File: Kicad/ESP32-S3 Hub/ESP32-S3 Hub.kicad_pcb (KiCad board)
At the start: 6 copper layers, 15 x 30 mm, 60 parts, among them J1 1.27mm 3pin socket, J10 1.27mm 3pin socket, J11 7 pin FPC 0.3mm Panasonic Y3b, J12 1.27mm 3pin socket, J13 TE 3-2363961-0 receptacle, J14 TE 3-2363962-0 Connector, J16 TE 3-2363961-0 receptacle, J17 TE 3-2363962-0 Connector, J2 1.27mm 3pin socket, J21 1.27mm 4 pin socket, J22 1.27mm 4 pin header, J3 7 pin FPC 0.3mm Panasonic Y3b, J4 1.27mm 3pin socket, J5 7 pin FPC 0.3mm Panasonic Y3b, J6 1.27mm 3pin socket, J7 1.27mm 3pin socket, J8 7 pin FPC 0.3mm Panasonic Y3b, J9 1.27mm 3pin socket, SW1 Mitsumi R-667996, SW2 Mitsumi R-667996, U1 ESP32-S3, U2 74HC595, U3 THVD1420DRLR, Y1 ABM11-40.000MHZ-B1U-T3, 10ppm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

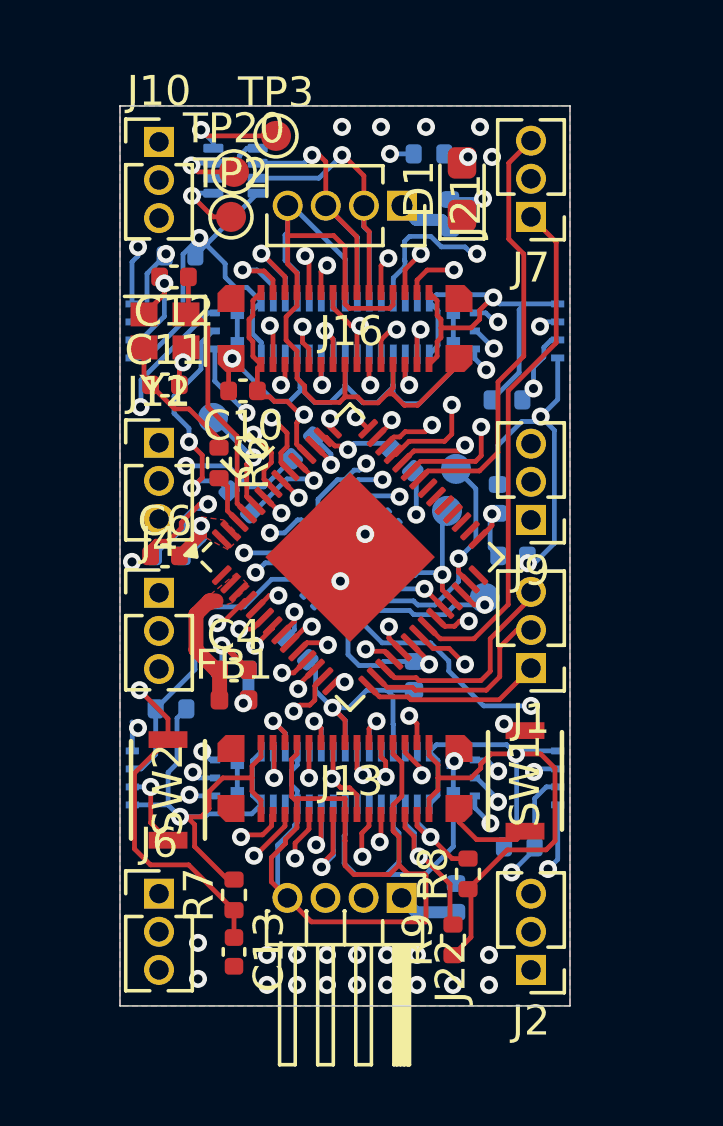
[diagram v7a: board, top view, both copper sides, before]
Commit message: Arranged Silkscreen
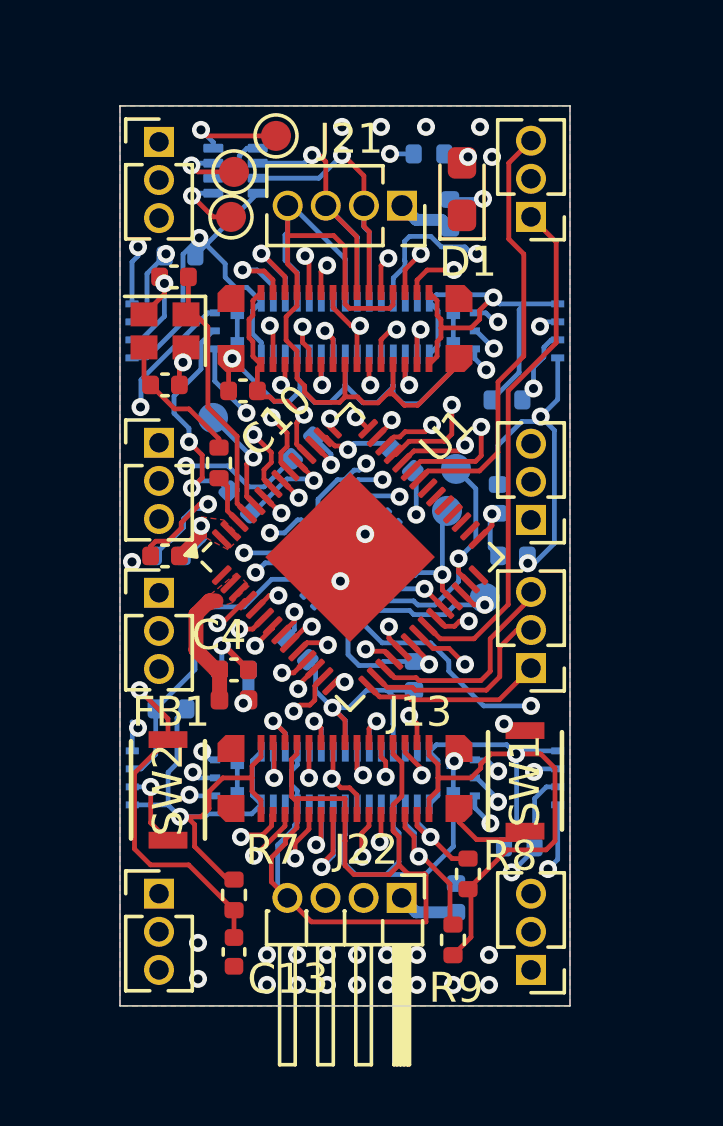
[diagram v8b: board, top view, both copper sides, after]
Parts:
- TP1: value ~ -> S-EN
- TP12: value ~ -> SRCLK
- TP14: value ~ -> SER
- TP2: value ~ -> RX
- TP3: value ~ -> TX
- TP4: value ~ -> IO46
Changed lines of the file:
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@@
 		(tags "LED handsolder")
 		(property "Reference" "D1"
-			(at 0 -1.43 90)
+			(at -2.425 0.2 180)
 			(layer "F.SilkS")
 			(effects
@@
 		(tags "Through hole angled pin header THT 1x04 1.27mm single row")
 		(property "Reference" "J22"
-			(at 2.4325 -1.635 90)
+			(at -1.6 1.19 180)
 			(layer "F.SilkS")
 			(effects
@@
 		(tags "capacitor")
 		(property "Reference" "C13"
-			(at 0 -1.16 90)
+			(at 0.9 -1.8 180)
 			(layer "F.SilkS")
 			(effects
@@
 		(tags "capacitor")
 		(property "Reference" "C10"
-			(at 0 -1.16 0)
+			(at -1.1 -1 45)
 			(layer "F.SilkS")
 			(effects
@@
 			(at 0 -1.448 0)
 			(layer "F.SilkS")
+			(hide yes)
 			(effects
 				(font
@@
 		(tags "resistor")
 		(property "Reference" "R8"
-			(at 0 -1.17 90)
+			(at 0.6 1.4 180)
 			(layer "F.SilkS")
 			(effects
@@
 			(at 0 -1.695 0)
 			(layer "F.SilkS")
+			(hide yes)
 			(effects
 				(font
@@
 			(at 0 -1.695 0)
 			(layer "F.SilkS")
+			(hide yes)
 			(effects
 				(font
@@
 		(tags "capacitor")
 		(property "Reference" "C4"
-			(at 0 -1.16 0)
+			(at -0.5 -1.16 0)
 			(layer "F.SilkS")
 			(effects
@@
 			(at 0 -1.448 0)
 			(layer "F.SilkS")
+			(hide yes)
 			(effects
 				(font
@@
 			)
 		)
-		(property "Value" "~"
+		(property "Value" "RX"
 			(at 0 1.55 0)
 			(layer "F.Fab")
@@
 			(at 0 -1.16 0)
 			(layer "F.SilkS")
+			(hide yes)
 			(effects
 				(font
@@
 			(at 0 -1.695 0)
 			(layer "F.SilkS")
+			(hide yes)
 			(effects
 				(font
@@
 			(at 0 -1.695 0)
 			(layer "F.SilkS")
+			(hide yes)
 			(effects
 				(font
@@
 		(tags "SMD SMT crystal")
 		(property "Reference" "Y1"
-			(at 0 -2.000001 0)
+			(at -1.8 -1.7 0)
 			(layer "F.SilkS")
+			(hide yes)
 			(effects
 				(font
@@
 			(at 0 -1.695 0)
 			(layer "F.SilkS")
+			(hide yes)
 			(effects
 				(font
@@
 		(tags "resistor")
 		(property "Reference" "R9"
-			(at 0 -1.17 90)
+			(at -1.6 0.1 180)
 			(layer "F.SilkS")
 			(effects
@@
 		(tags "inductor")
 		(property "Reference" "FB1"
-			(at 0 -1.17 0)
+			(at -2.1 0.4 0)
 			(layer "F.SilkS")
 			(effects
@@
 		(tags "QFN NoLead")
 		(property "Reference" "U1"
-			(at 0 -4.800001 45)
+			(at 5.140986 -0.573076 45)
 			(layer "F.SilkS")
 			(effects
@@
 			(at 0 -1.16 0)
 			(layer "F.SilkS")
+			(hide yes)
 			(effects
 				(font
@@
 			(at 0 -1.695 0)
 			(layer "F.SilkS")
+			(hide yes)
 			(effects
 				(font
@@
 		(tags "mezzanine B2B 0.4mm board-to-board receptacle")
 		(property "Reference" "J16"
-			(at 0.21 0.01 0)
+			(at 2.3 2.3 0)
 			(unlocked yes)
 			(layer "F.SilkS")
+			(hide yes)
 			(effects
 				(font
@@
 		(tags "Through hole socket strip THT 1x04 1.27mm single row")
 		(property "Reference" "J21"
-			(at 0 -2.135 90)
+			(at -2.225 1.7 180)
 			(layer "F.SilkS")
 			(effects
@@
 		(tags "resistor")
 		(property "Reference" "R7"
-			(at 0 -1.17 90)
+			(at 1.5 1.3 180)
 			(layer "F.SilkS")
 			(effects
@@
 		(tags "resistor")
 		(property "Reference" "R6"
-			(at 0 -1.17 90)
+			(at -1.5 1.1 180)
 			(layer "F.SilkS")
+			(hide yes)
 			(effects
 				(font
@@
 			(at 0 -1.695 0)
 			(layer "F.SilkS")
+			(hide yes)
 			(effects
 				(font
@@
 			(at 0 -1.695 0)
 			(layer "F.SilkS")
+			(hide yes)
 			(effects
 				(font
@@
 		(tags "capacitor")
 		(property "Reference" "C6"
-			(at 0 -1.16 360)
+			(at 0.9 1.1 90)
 			(layer "F.SilkS")
+			(hide yes)
 			(effects
 				(font
@@
 			(at 0 -1.448 0)
 			(layer "F.SilkS")
+			(hide yes)
 			(effects
 				(font
@@
 			)
 		)
-		(property "Value" "~"
+		(property "Value" "TX"
 			(at 0 1.55 0)
 			(layer "F.Fab")
@@
 		(tags "mezzanine B2B 0.4mm board-to-board receptacle")
 		(property "Reference" "J13"
-			(at 0.21 0.01 0)
+			(at 2.5 -2.3 0)
 			(unlocked yes)
 			(layer "F.SilkS")
@@
 		(tags "resistor")
 		(property "Reference" "R1"
-			(at 0 1.17 135)
+			(at 1.697056 0 135)
 			(layer "B.SilkS")
 			(effects
@@
 		(tags "resistor")
 		(property "Reference" "R10"
-			(at 0 1.17 0)
+			(at -2.3 -0.3 0)
 			(layer "B.SilkS")
 			(effects
@@
 		(tags "DHVQFN NoLead")
 		(property "Reference" "U2"
-			(at 0 3.05 135)
+			(at 2.687006 0.141421 -135)
 			(layer "B.SilkS")
 			(effects
@@
 		(tags "capacitor")
 		(property "Reference" "C9"
-			(at 0 1.16 0)
+			(at 1.5 0.1 90)
 			(layer "B.SilkS")
 			(effects
@@
 		(tags "capacitor")
 		(property "Reference" "C2"
-			(at 0 1.16 0)
+			(at -0.3 1.5 0)
 			(layer "B.SilkS")
 			(effects
@@
 		(tags "resistor")
 		(property "Reference" "R3"
-			(at 0 1.17 135)
+			(at -2.05061 0.070711 135)
 			(layer "B.SilkS")
 			(effects
@@
 			(at 0 1.448 0)
 			(layer "B.SilkS")
+			(hide yes)
 			(effects
 				(font
@@
 			)
 		)
-		(property "Value" "~"
+		(property "Value" "IO46"
 			(at 0 -1.55 0)
 			(layer "B.Fab")
@@
 		(tags "capacitor")
 		(property "Reference" "C7"
-			(at 0 1.16 90)
+			(at 1.8 0 90)
 			(layer "B.SilkS")
 			(effects
@@
 		(tags "resistor")
 		(property "Reference" "R20"
-			(at 0 1.17 0)
+			(at -2.3 0 0)
 			(layer "B.SilkS")
 			(effects
@@
 			(at 0 1.448 0)
 			(layer "B.SilkS")
+			(hide yes)
 			(effects
 				(font
@@
 			)
 		)
-		(property "Value" "~"
+		(property "Value" "SER"
 			(at 0 -1.55 0)
 			(layer "B.Fab")
@@
 		(tags "capacitor")
 		(property "Reference" "C8"
-			(at 0 1.16 90)
+			(at 0 -1.2 90)
 			(layer "B.SilkS")
 			(effects
@@
 		(tags "mezzanine B2B 0.4mm board-to-board connector")
 		(property "Reference" "J17"
-			(at 0.04 -2.33 0)
+			(at -0.2 2.3 0)
 			(unlocked yes)
 			(layer "B.SilkS")
@@
 			(at 0 1.448 0)
 			(layer "B.SilkS")
+			(hide yes)
 			(effects
 				(font
@@
 			)
 		)
-		(property "Value" "~"
+		(property "Value" "S-EN"
 			(at 0 -1.55 0)
 			(layer "B.Fab")
@@
 		(tags "resistor")
 		(property "Reference" "R19"
-			(at 0 1.17 0)
+			(at -2.3 -0.1 0)
 			(layer "B.SilkS")
 			(effects
@@
 			(at 0 1.448 0)
 			(layer "B.SilkS")
+			(hide yes)
 			(effects
 				(font
@@
 			)
 		)
-		(property "Value" "~"
+		(property "Value" "SRCLK"
 			(at 0 -1.55 0)
 			(layer "B.Fab")
@@
 		(tags "capacitor")
 		(property "Reference" "C14"
-			(at 0 1.16 90)
+			(at -1.7 0 180)
 			(layer "B.SilkS")
 			(effects
@@
 		(tags "SOT-583-8")
 		(property "Reference" "U3"
-			(at 0 2.2 180)
+			(at 2.15 -0.16 180)
 			(unlocked yes)
 			(layer "B.SilkS")
@@
 		(tags "resistor")
 		(property "Reference" "R18"
-			(at 0 1.17 0)
+			(at -0.7 1.9 90)
 			(layer "B.SilkS")
 			(effects
@@
 		(tags "capacitor")
 		(property "Reference" "C5"
-			(at 0 1.16 0)
+			(at -1.8 0.1 0)
 			(layer "B.SilkS")
 			(effects
@@
 		(tags "capacitor")
 		(property "Reference" "C3"
-			(at 0 1.16 0)
+			(at -1.7 -0.7 0)
 			(layer "B.SilkS")
 			(effects
